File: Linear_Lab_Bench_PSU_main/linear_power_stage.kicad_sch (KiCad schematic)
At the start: 46 parts, among them J2 Conn_01x10_Male, Q11 2N5550, Q12 IXTH48P20P, Q13 2N5550, U2 LM324, U3 LTC1051

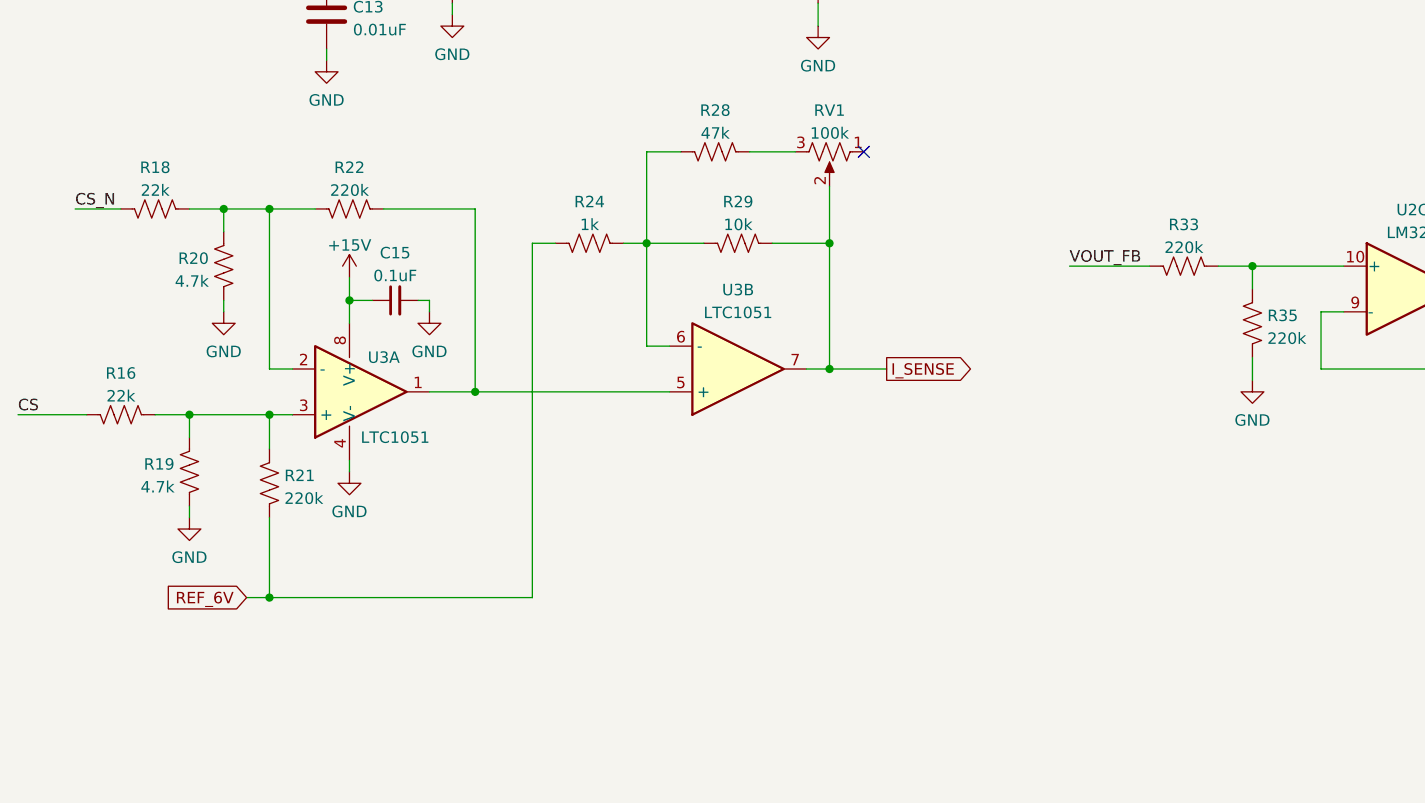
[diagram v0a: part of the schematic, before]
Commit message: Notes on schematic for resistor changes
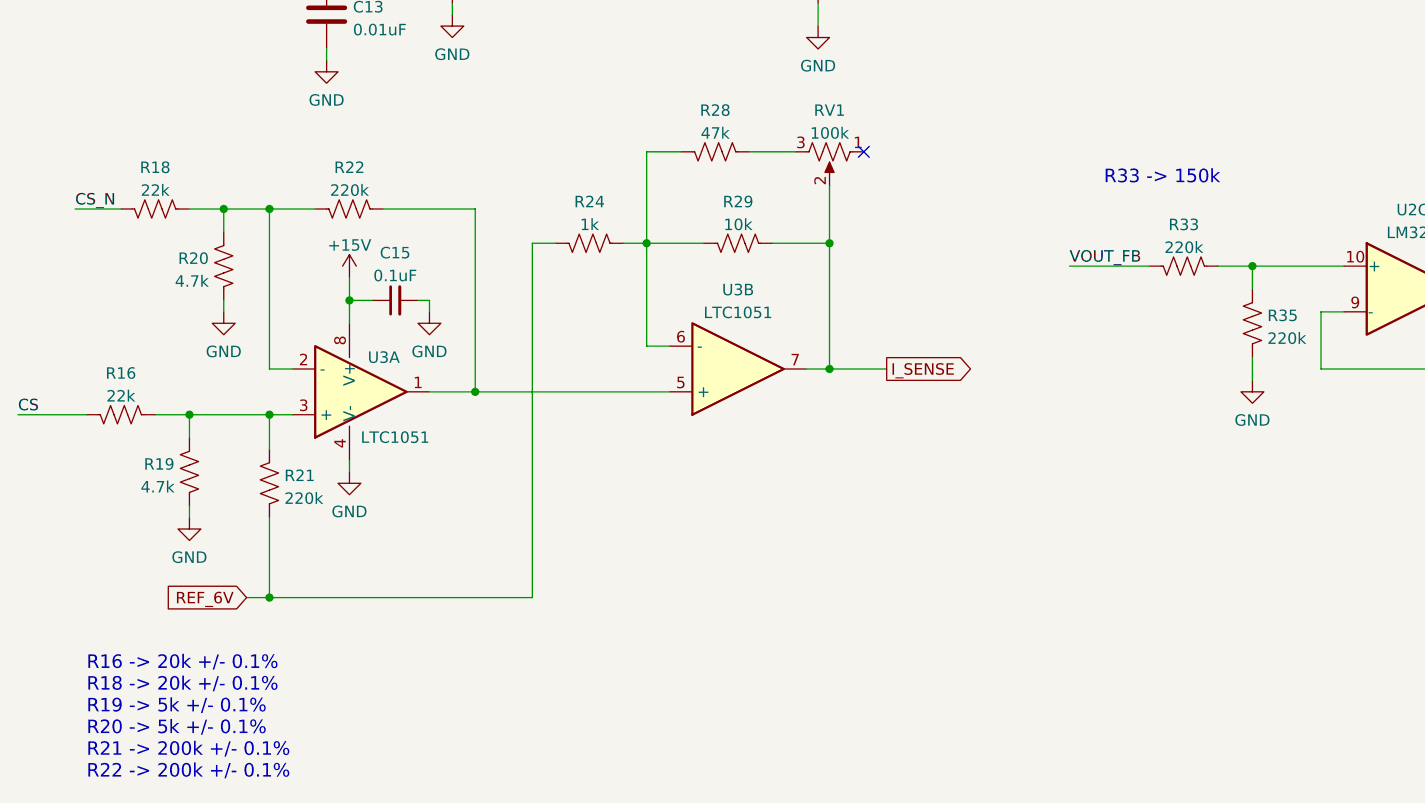
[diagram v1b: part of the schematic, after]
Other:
- note added: "R16 -> 20k +/- 0.1% R18 -> 20k +/- 0.1% R19 -> 5k +/- 0.1% R20 -> 5k +/- 0.1% R21 -> 200k +/- 0.1% R22 -> 200k +/- 0.1%"
- note added: "R33 -> 150k"
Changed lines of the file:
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@@
     (stroke (width 0) (type default) (color 0 0 0 0))
+  )
+  (text "R33 -> 150k" (at 146.05 109.22 0)
+    (effects (font (size 1.5 1.5)) (justify left bottom))
+  )
+  (text "R16 -> 20k +/- 0.1%\nR18 -> 20k +/- 0.1%\nR19 -> 5k +/- 0.1%\nR20 -> 5k +/- 0.1%\nR21 -> 200k +/- 0.1%\nR22 -> 200k +/- 0.1%"
+    (at 33.02 175.26 0)
+    (effects (font (size 1.5 1.5)) (justify left bottom))
   )
   (label "CS_N" (at 31.75 111.76 0)
